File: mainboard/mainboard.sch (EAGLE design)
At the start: 51 parts, among them IC1 ATMEGA168-PU, IC6 LM317MSTT3

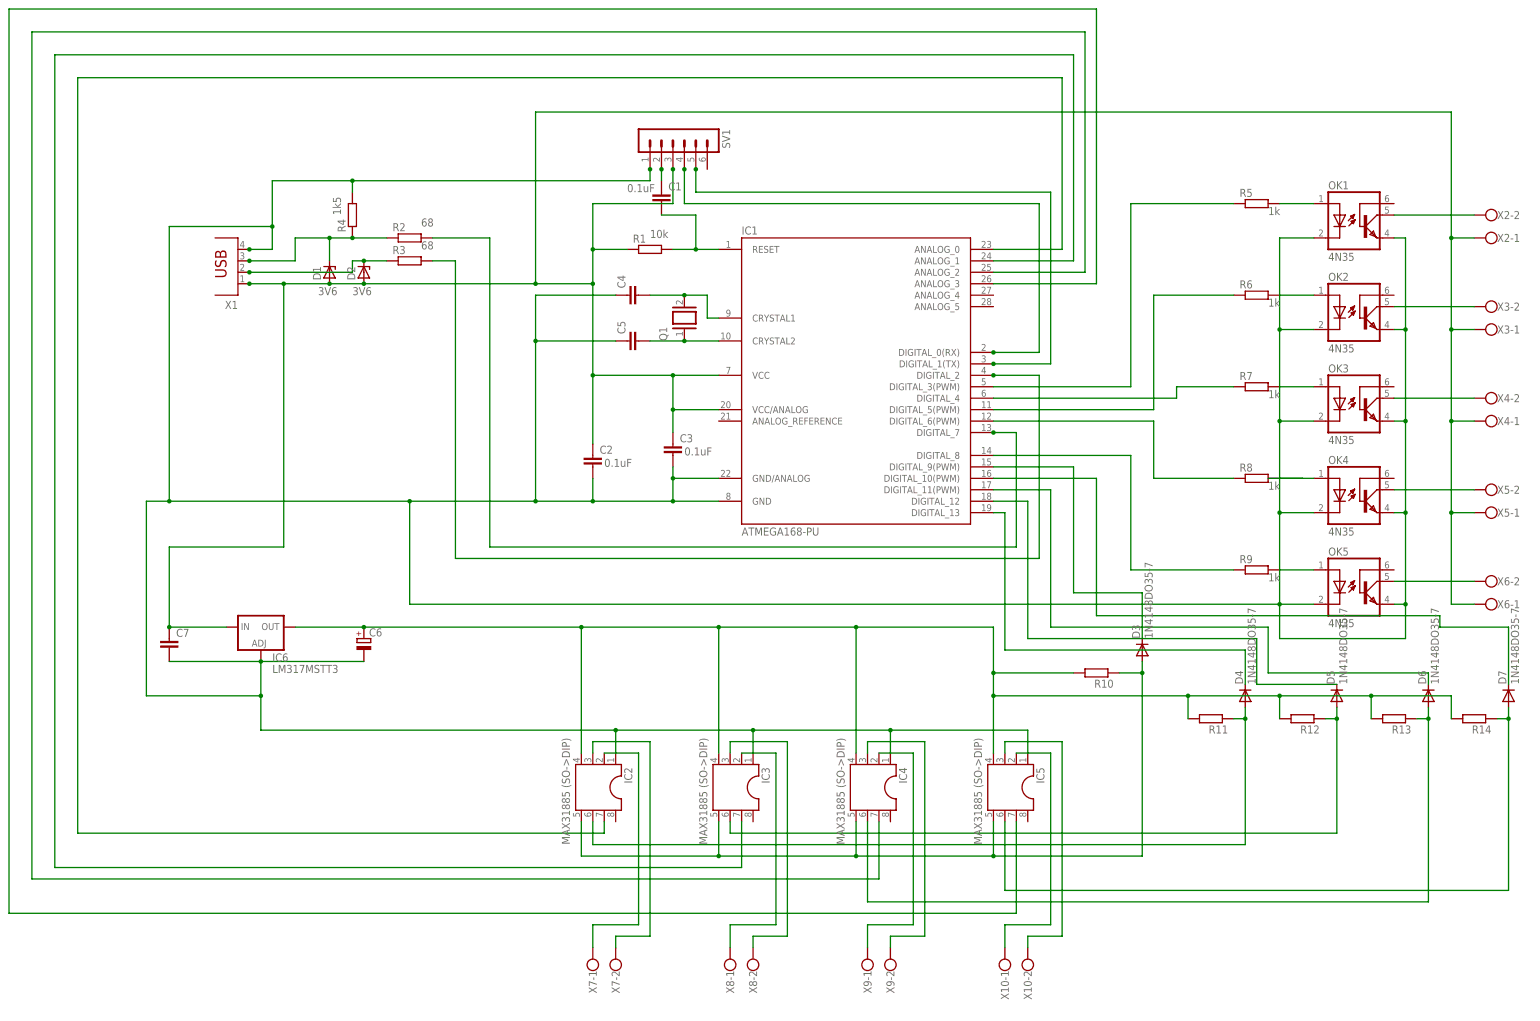
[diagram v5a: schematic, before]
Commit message: added values to components
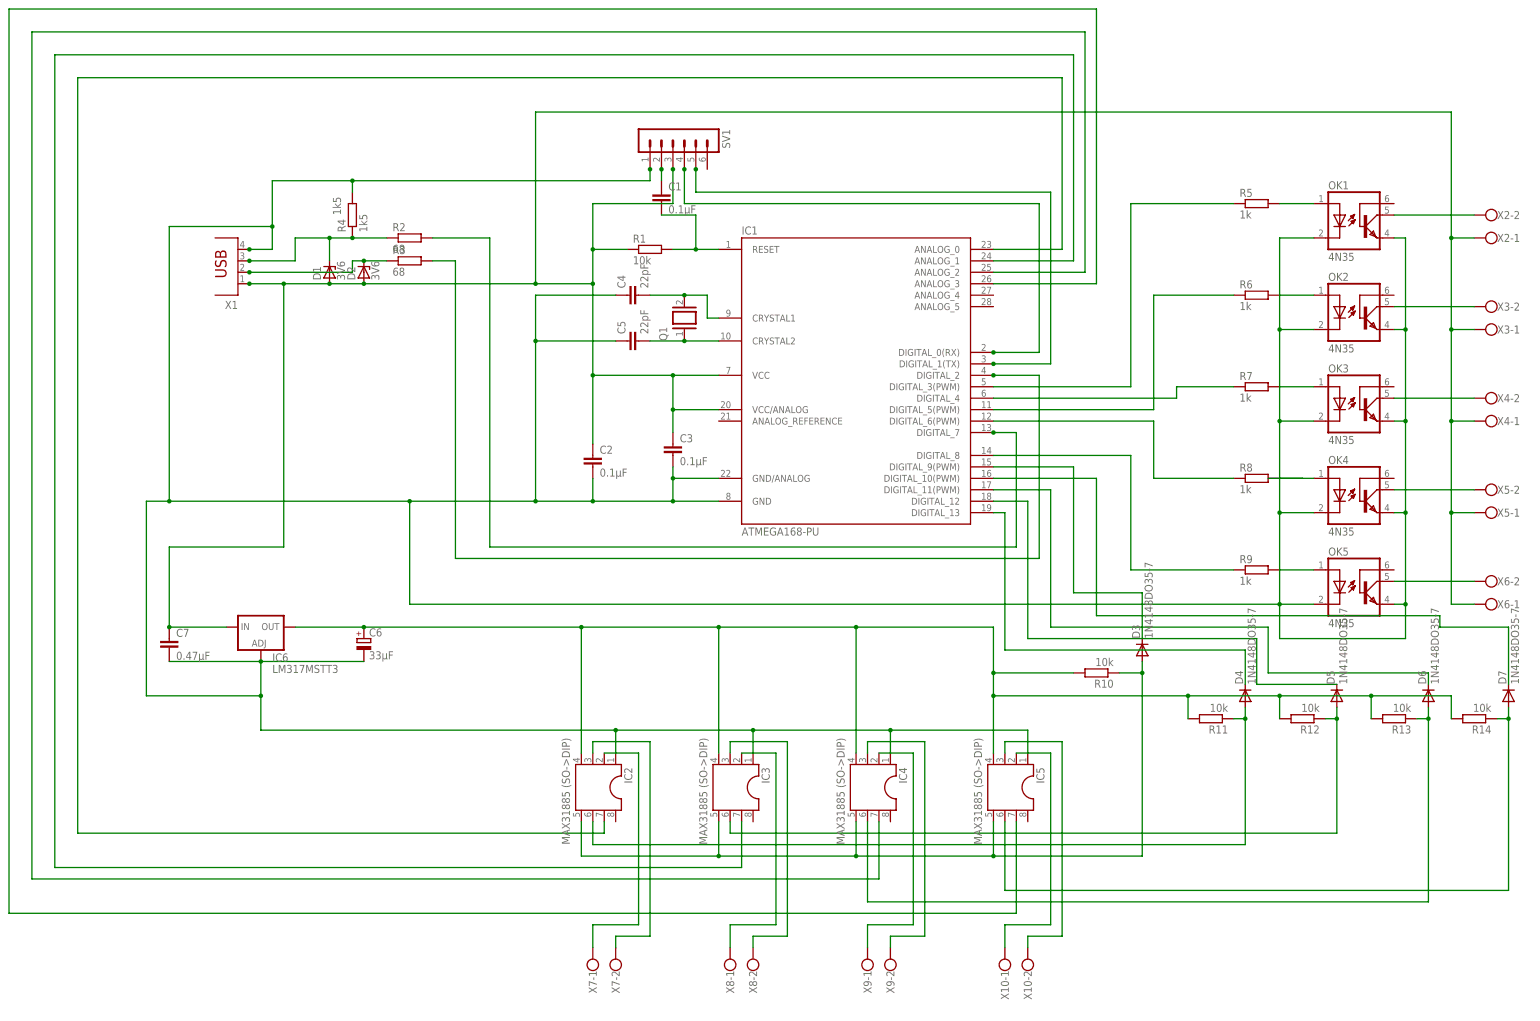
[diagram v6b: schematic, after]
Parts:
- C1, C2, C3: value (none) -> 0.1μF
- C4, C5: value (none) -> 22pF
- C6: value (none) -> 33μF
- C7: value (none) -> 0.47μF
- D1, D2: value (none) -> 3V6
- R1, R10, R11, R12, R13, R14: value (none) -> 10k
- R2, R3: value (none) -> 68
- R4: value (none) -> 1k5
- R5, R6, R7, R8, R9: value (none) -> 1k
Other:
- note removed: "0.1uF"
- note removed: "10k"
- note removed: "1k"
- note removed: "3V6"
- note removed: "68"
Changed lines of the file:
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@@
 <parts>
 <part name="IC1" library="Arduino-AVR" deviceset="ATMEGA168-PU" device=""/>
-<part name="R1" library="resistor" deviceset="R-EU_" device="0204/7"/>
-<part name="C2" library="capacitor-wima" deviceset="C" device="2,5-3"/>
-<part name="C3" library="capacitor-wima" deviceset="C" device="2,5-3"/>
+<part name="R1" library="resistor" deviceset="R-EU_" device="0204/7" value="10k"/>
+<part name="C2" library="capacitor-wima" deviceset="C" device="2,5-3" value="0.1μF"/>
+<part name="C3" library="capacitor-wima" deviceset="C" device="2,5-3" value="0.1μF"/>
 <part name="SV1" library="con-lstb" deviceset="MA06-1" device=""/>
-<part name="C1" library="capacitor-wima" deviceset="C" device="2,5-3"/>
+<part name="C1" library="capacitor-wima" deviceset="C" device="2,5-3" value="0.1μF"/>
 <part name="X1" library="con-berg" deviceset="PN61729" device=""/>
-<part name="R2" library="resistor" deviceset="R-EU_" device="0204/7"/>
-<part name="R3" library="resistor" deviceset="R-EU_" device="0204/7"/>
-<part name="R4" library="resistor" deviceset="R-EU_" device="0204/7"/>
-<part name="D1" library="diode" deviceset="ZENER-DIODE" device="ZD-5"/>
-<part name="D2" library="diode" deviceset="ZENER-DIODE" device="ZD-5"/>
+<part name="R2" library="resistor" deviceset="R-EU_" device="0204/7" value="68"/>
+<part name="R3" library="resistor" deviceset="R-EU_" device="0204/7" value="68"/>
+<part name="R4" library="resistor" deviceset="R-EU_" device="0204/7" value="1k5"/>
+<part name="D1" library="diode" deviceset="ZENER-DIODE" device="ZD-5" value="3V6"/>
+<part name="D2" library="diode" deviceset="ZENER-DIODE" device="ZD-5" value="3V6"/>
 <part name="Q1" library="special" deviceset="XTAL/S" device=""/>
-<part name="C4" library="capacitor-wima" deviceset="C" device="2,5-3"/>
-<part name="C5" library="capacitor-wima" deviceset="C" device="2,5-3"/>
+<part name="C4" library="capacitor-wima" deviceset="C" device="2,5-3" value="22pF"/>
+<part name="C5" library="capacitor-wima" deviceset="C" device="2,5-3" value="22pF"/>
 <part name="OK1" library="optocoupler" deviceset="4N35" device=""/>
 <part name="OK2" library="optocoupler" deviceset="4N35" device=""/>
@@
 <part name="OK4" library="optocoupler" deviceset="4N35" device=""/>
 <part name="OK5" library="optocoupler" deviceset="4N35" device=""/>
-<part name="R5" library="resistor" deviceset="R-EU_" device="0204/7"/>
-<part name="R6" library="resistor" deviceset="R-EU_" device="0204/7"/>
-<part name="R7" library="resistor" deviceset="R-EU_" device="0204/7"/>
-<part name="R8" library="resistor" deviceset="R-EU_" device="0204/7"/>
-<part name="R9" library="resistor" deviceset="R-EU_" device="0204/7"/>
+<part name="R5" library="resistor" deviceset="R-EU_" device="0204/7" value="1k"/>
+<part name="R6" library="resistor" deviceset="R-EU_" device="0204/7" value="1k"/>
+<part name="R7" library="resistor" deviceset="R-EU_" device="0204/7" value="1k"/>
+<part name="R8" library="resistor" deviceset="R-EU_" device="0204/7" value="1k"/>
+<part name="R9" library="resistor" deviceset="R-EU_" device="0204/7" value="1k"/>
 <part name="X2" library="con-wago-500" deviceset="W237-102" device=""/>
 <part name="X3" library="con-wago-500" deviceset="W237-102" device=""/>
@@
 <part name="IC5" library="ic-package" deviceset="DIL8" device="S"/>
 <part name="IC6" library="v-reg-mod" deviceset="LM317?*" device="MSTT3"/>
-<part name="C6" library="resistor" deviceset="CPOL-EU" device="153CLV-0605"/>
-<part name="C7" library="capacitor-wima" deviceset="C" device="2,5-3"/>
+<part name="C6" library="resistor" deviceset="CPOL-EU" device="153CLV-0605" value="33μF"/>
+<part name="C7" library="capacitor-wima" deviceset="C" device="2,5-3" value="0.47μF"/>
 <part name="X7" library="con-wago-500" deviceset="W237-102" device=""/>
 <part name="X8" library="con-wago-500" deviceset="W237-102" device=""/>
 <part name="X9" library="con-wago-500" deviceset="W237-102" device=""/>
 <part name="X10" library="con-wago-500" deviceset="W237-102" device=""/>
-<part name="R10" library="resistor" deviceset="R-EU_" device="0204/7"/>
+<part name="R10" library="resistor" deviceset="R-EU_" device="0204/7" value="10k"/>
 <part name="D3" library="diode" deviceset="1N4148" device="DO35-7"/>
-<part name="R11" library="resistor" deviceset="R-EU_" device="0204/7"/>
+<part name="R11" library="resistor" deviceset="R-EU_" device="0204/7" value="10k"/>
 <part name="D4" library="diode" deviceset="1N4148" device="DO35-7"/>
-<part name="R12" library="resistor" deviceset="R-EU_" device="0204/7"/>
+<part name="R12" library="resistor" deviceset="R-EU_" device="0204/7" value="10k"/>
 <part name="D5" library="diode" deviceset="1N4148" device="DO35-7"/>
-<part name="R13" library="resistor" deviceset="R-EU_" device="0204/7"/>
+<part name="R13" library="resistor" deviceset="R-EU_" device="0204/7" value="10k"/>
 <part name="D6" library="diode" deviceset="1N4148" device="DO35-7"/>
-<part name="R14" library="resistor" deviceset="R-EU_" device="0204/7"/>
+<part name="R14" library="resistor" deviceset="R-EU_" device="0204/7" value="10k"/>
 <part name="D7" library="diode" deviceset="1N4148" device="DO35-7"/>
 </parts>
@@
 <sheet>
 <plain>
-<text x="-5.08" y="58.42" size="1.778" layer="96">68</text>
-<text x="-5.08" y="53.34" size="1.778" layer="96">68</text>
 <text x="-22.86" y="60.96" size="1.778" layer="96" rot="R90">1k5</text>
-<text x="45.72" y="55.88" size="1.778" layer="96">10k</text>
-<text x="35.56" y="5.08" size="1.778" layer="96">0.1uF</text>
-<text x="53.34" y="7.62" size="1.778" layer="96">0.1uF</text>
-<text x="40.64" y="66.04" size="1.778" layer="96">0.1uF</text>
-<text x="-27.94" y="43.18" size="1.778" layer="96">3V6</text>
-<text x="-20.32" y="43.18" size="1.778" layer="96">3V6</text>
-<text x="182.88" y="60.96" size="1.778" layer="96">1k</text>
-<text x="182.88" y="40.64" size="1.778" layer="96">1k</text>
-<text x="182.88" y="20.32" size="1.778" layer="96">1k</text>
-<text x="182.88" y="0" size="1.778" layer="96">1k</text>
-<text x="182.88" y="-20.32" size="1.778" layer="96">1k</text>
 <text x="27.94" y="-78.74" size="1.778" layer="96" rot="R90">MAX31885 (SO-&gt;DIP)</text>
 <text x="58.42" y="-78.74" size="1.778" layer="96" rot="R90">MAX31885 (SO-&gt;DIP)</text>
